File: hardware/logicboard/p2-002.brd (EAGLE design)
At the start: 72 x 72 mm, 18 parts, among them IC1 74LS07N, U1 DS18B20

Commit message: Writing.
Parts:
- removed H1, H2: STAND-OFF, SparkFun-Hardware:STAND-OFF
- removed JP2: RTC, SparkFun-Connectors:1X05
- added J0: (no value), con-jack:SPC4077
- added J1, J2: DIN5, SparkFun-Connectors:DIN5-RA-PTH
- added SV1: (no value), con-ml:ML10L
- moved RN1 42.3 mm to (12.0, 61.5)
- moved C7 41.3 mm to (20.0, 4.50)
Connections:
- removed net V+: JP5.3
- net GND: now also J0.1, J0.2, J2.2; no longer JP2.2
- net MIRTN: now also J1.5
- net MISND: now also J1.4
- net MTRTN: now also J2.5
- net MTSND: now also J2.4
- net SCL: no longer JP2.4
- net SDA: no longer JP2.5
- net VCC: no longer JP2.1
- net VIN: now also J0.3, JP5.3
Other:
- board text removed: "(OUT2)"
- board text removed: "10k"
- board text removed: "5V"
- board text removed: "G"
- board text removed: "NC"
- board text removed: "RTC1"
- board text removed: "SC"
- board text removed: "SD"
- board text removed: "SparkFun Real Time Clock Module (12708)"

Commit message: Wiring.
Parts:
- removed C6, C7: 10n, resistor:C025-024X044
- RN3: value 220 -> (none)
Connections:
- new net N$1: IC1.4, RN3.5
- new net N$2: IC1.6, RN3.7
- net GND: now also SV1.8; no longer C6.2, C7.2
- net GPIO1: now also SV1.1
- net GPIO2: now also SV1.7
- net MISO: now also SV1.3
- net MOSI: now also SV1.6
- net RX: now also IC1.3, IC1.5
- net SCK: now also SV1.5
- net VCC: now also RN3.4, RN3.6, SV1.4; no longer C6.1, C7.1

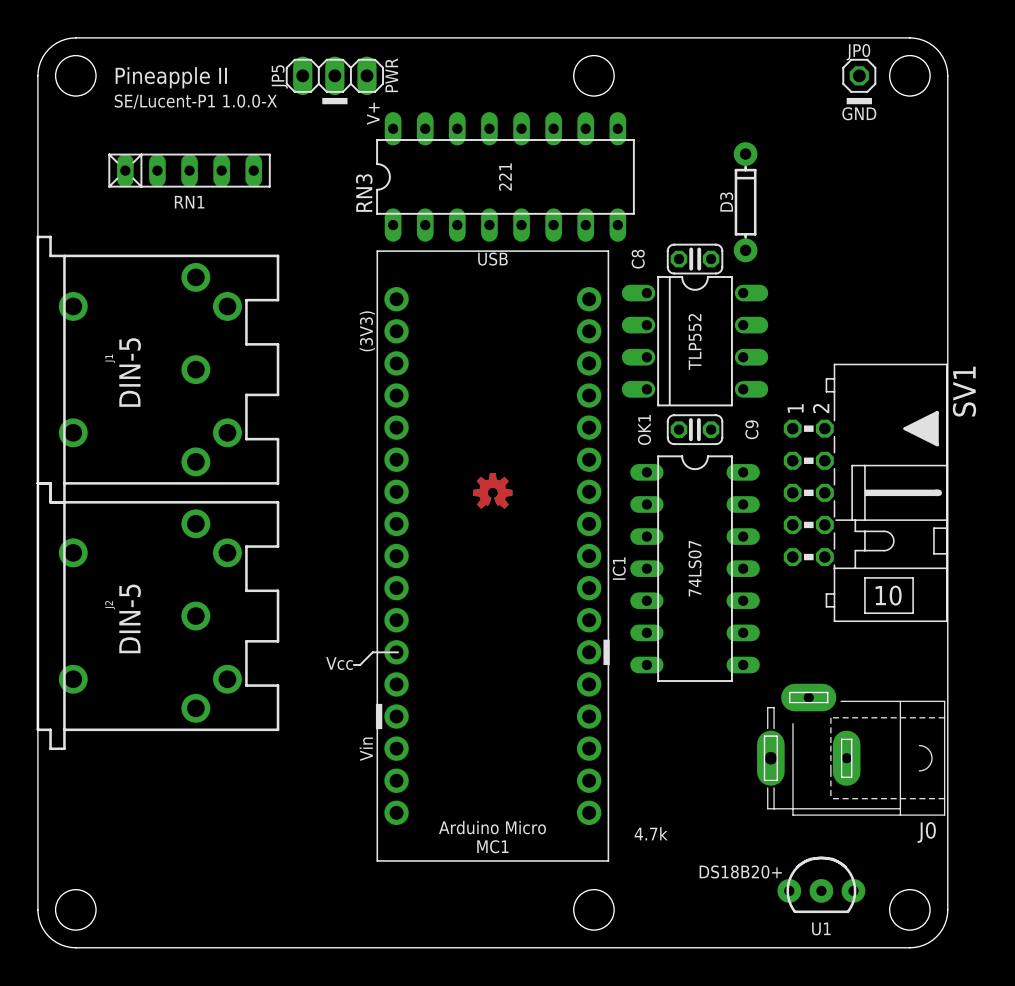
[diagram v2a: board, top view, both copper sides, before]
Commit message: First working version of MIDI IN, MIDI THRU, SPI edition.
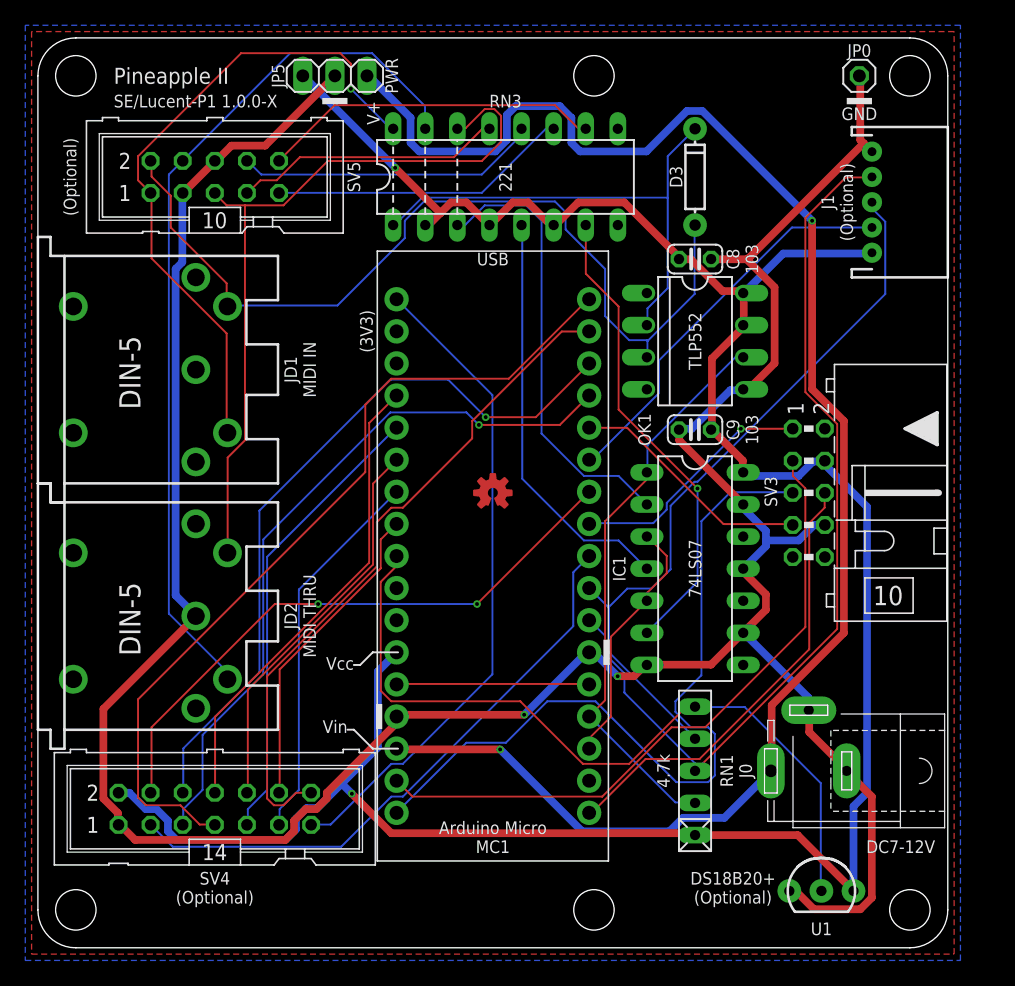
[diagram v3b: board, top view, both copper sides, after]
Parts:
- added JD1: DIN5, SparkFun-Connectors:DIN5-RA-PTH
- added SV4: (no value), con-ml:ML14
- added SV5: (no value), con-ml:ML10
- J1: value DIN5 -> (none); device SparkFun-Connectors:DIN5-RA-PTH -> SparkFun-Connectors:JST-5-PTH
- moved J1 67.3 mm to (66.0, 59.0)
- moved RN1 62.1 mm to (52.0, 14.0), turned to 90 degrees
- moved D3 4.47 mm to (52.0, 61.0)
- moved J0 1.00 mm to (61.0, 14.0)
- renumbered J2 to JD2, SV1 to SV3
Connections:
- net N$1 renamed MO
- net N$2 renamed MO2
- new net MO2RTN: RN3.10, SV5.10
- new net MO2SND: RN3.11, SV5.9
- new net MORTN: RN3.12, SV5.8
- new net MOSND: RN3.13, SV5.7
- net ANLG1: now also SV4.8
- net ANLG2: now also SV4.9
- net ANLG3: now also SV4.10
- net ANLG4: now also SV4.11
- net D7: now also J1.4
- net DTCT1: now also SV4.4
- net DTCT2: now also SV4.5
- net DTCT3: now also SV4.6
- net DTCT4: now also SV4.7
- net GATE: now also SV4.12
- net GND: now also J1.1, SV4.1, SV5.3, SV5.6
- net LED0: now also SV4.13
- net LED1: now also SV4.14
- net MIRTN: now also JD1.5, SV5.2; no longer J1.5
- net MISND: now also JD1.4, SV5.1; no longer J1.4
- net MTRTN: now also SV5.5
- net MTSND: now also SV5.4
- net RLY: now also SV4.3
- net RX: no longer IC1.3, IC1.5
- net SCL: now also J1.3
- net SDA: now also J1.2
- net TX: now also IC1.3, IC1.5
- net VCC: now also J1.5, SV4.2
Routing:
- net GND: track 0.00 -> 229.8 mm, vias 0 -> 2
- net VCC: track 0.00 -> 196.2 mm, vias 0 -> 2
- net VIN: track 0.00 -> 130.4 mm, vias 0 -> 2
- net SDA: track 0.00 -> 71.5 mm
- net MIRTN: track 0.00 -> 71.2 mm
- net MTSND: track 0.00 -> 69.7 mm
- net DTCT4: track 0.00 -> 66.7 mm
- net SCK: track 0.00 -> 63.0 mm
- net THS: track 0.00 -> 61.3 mm
- net MTRTN: track 0.00 -> 59.6 mm
- net SCL: track 0.00 -> 58.2 mm
- net DTCT3: track 0.00 -> 58.2 mm, vias 0 -> 1
- net DTCT2: track 0.00 -> 56.6 mm, vias 0 -> 1
- net LED1: track 0.00 -> 53.4 mm
- net LED0: track 0.00 -> 52.1 mm
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- added copper zone on layer 1, net GND
- added copper zone on layer 16, net GND
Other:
- board text added: "(Optional)"
- board text added: "103"
- board text added: "DC7-12V"
- board text added: "MIDI IN"
- board text added: "MIDI THRU"
- board text added: "STEPPER"
- board text added: "THRU"

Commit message: Arrangement of some parts (P20).
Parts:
- moved J0 1.00 mm to (61.0, 13.0)
- moved RN1 1.00 mm to (52.0, 13.0)
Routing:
- net GND: track 229.8 -> 256.2 mm
- net VIN: track 130.4 -> 107.8 mm
- net SCK: track 63.0 -> 49.5 mm, vias 0 -> 1
- net LED1: track 53.4 -> 66.5 mm
- net MISND: track 52.0 -> 42.8 mm, vias 1 -> 0
- net DTCT3: track 58.2 -> 67.4 mm
- net MTRTN: track 59.6 -> 51.3 mm
- net MIRTN: track 71.2 -> 79.1 mm, vias 0 -> 1
- net MO2RTN: track 26.9 -> 34.4 mm
- net THS: track 61.3 -> 67.8 mm
- net MT: track 35.3 -> 28.9 mm
- net LED0: track 52.1 -> 46.0 mm
- net DTCT1: track 47.6 -> 52.7 mm, vias 2 -> 1
- net MTSND: track 69.7 -> 66.0 mm
- net DTCT2: track 56.6 -> 59.9 mm
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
